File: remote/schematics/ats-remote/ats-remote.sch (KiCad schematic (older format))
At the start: 9 parts, among them J1 Conn_01x08, J2 Conn_01x08, J3 Conn_01x07, J4 Conn_01x07, J5 Conn_01x09, J6 Conn_01x09, U1 RFM95W-915S2, U2 PIC18F06Q40, U3 YIC71009EBGG

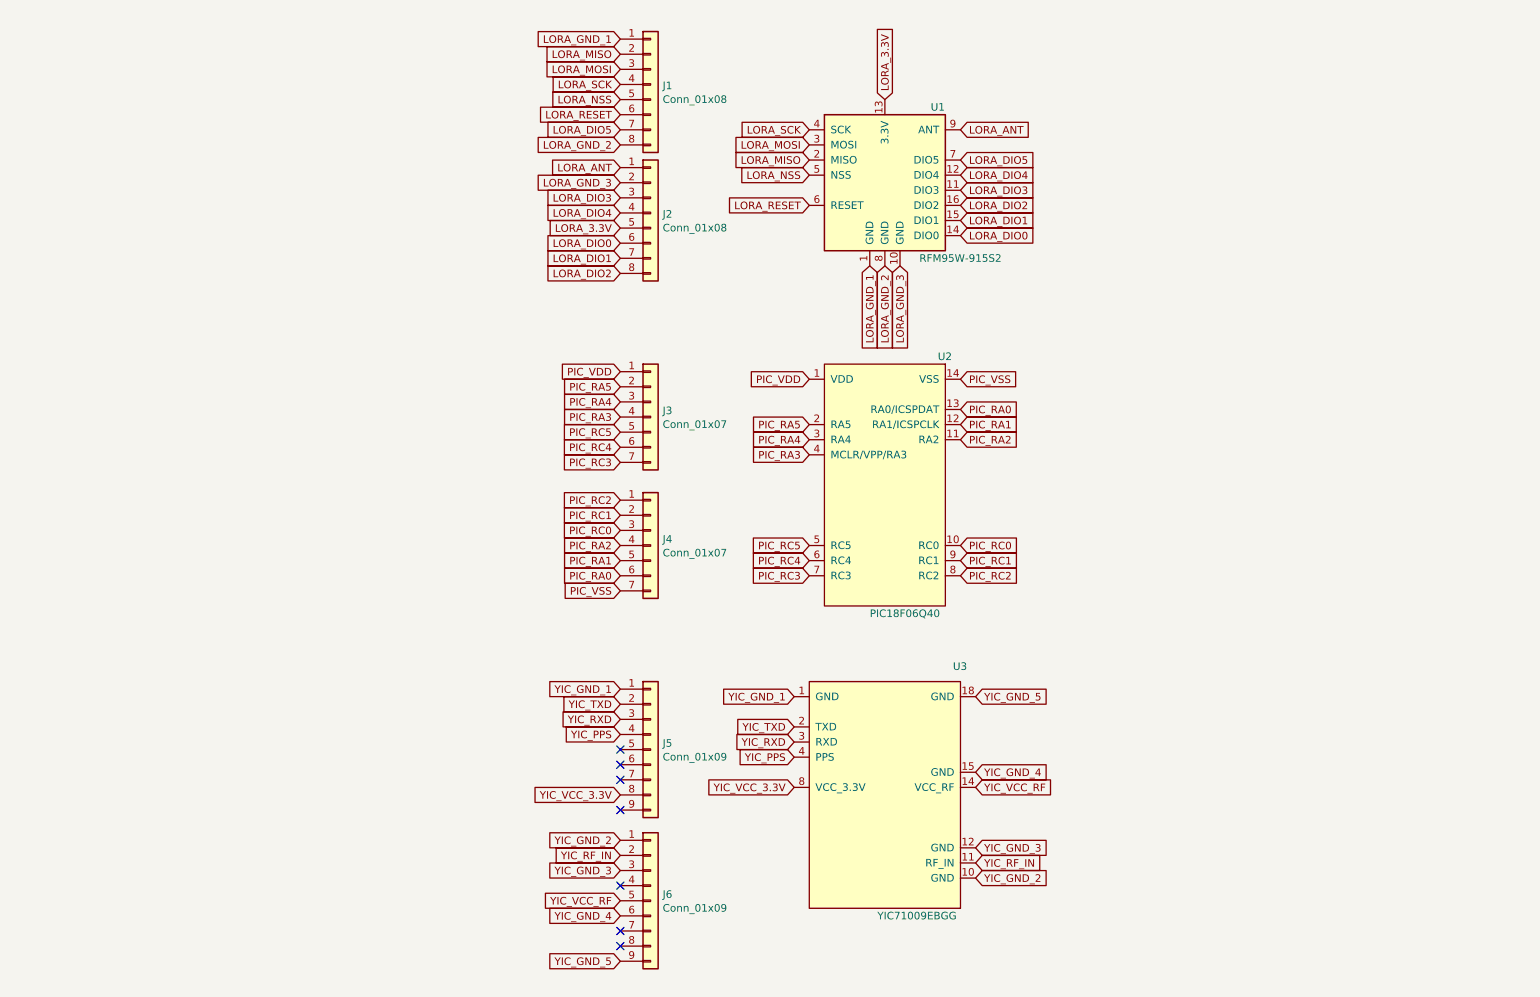
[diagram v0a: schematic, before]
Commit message: move remote schematic and pcb to v0.2.0 (#2)
v0.2.0

- 3.3v power and ground header
    - No OVP
    - No OCP
    - No polarity protection
    - Modules have their own decoupling caps
    - Modules have decoupling capacitors
- SPI header for LoRa module debug
- UART header for GPS module debug
- ICSP header for programming the PIC18
- LoRa module and SMD antenna
- GPS module and SMD antenna
- PIC18 controller
    - Controls SPI and UART
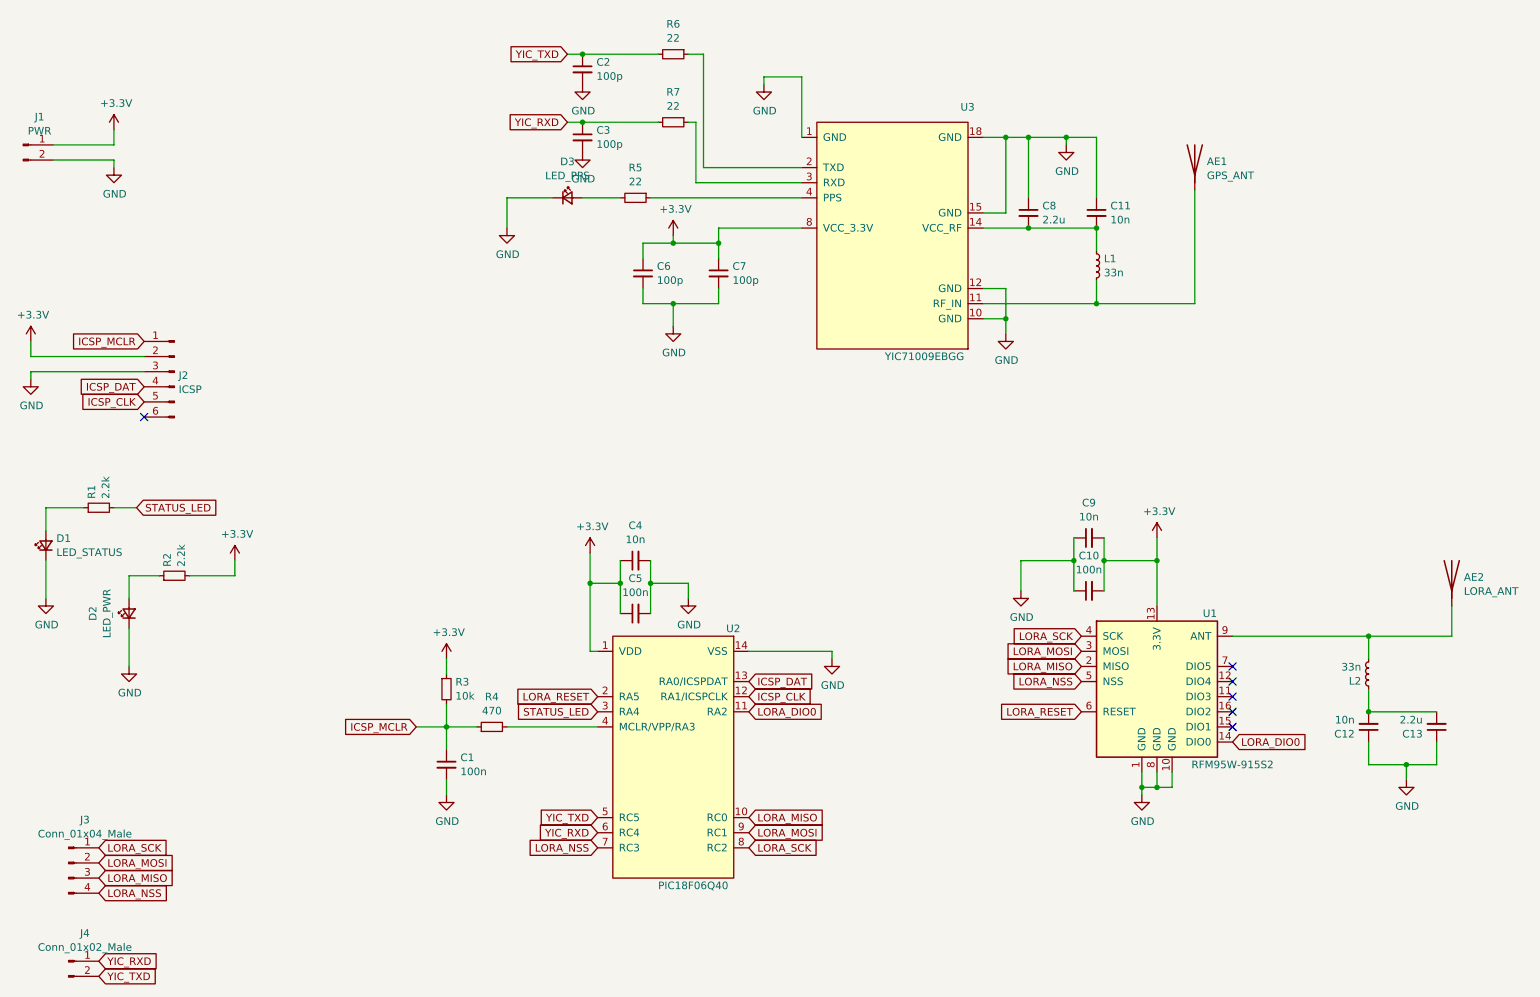
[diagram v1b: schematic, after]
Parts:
- removed J1, J2: Conn_01x08, Connector_PinSocket_1.27mm:PinSocket_1x08_P1.27mm_Vertical, symbol Connector_Generic:Conn_01x08
- removed J3, J4: Conn_01x07, Connector_PinSocket_1.27mm:PinSocket_1x07_P1.27mm_Vertical, symbol Connector_Generic:Conn_01x07
- removed J5, J6: Conn_01x09, Connector_PinSocket_1.27mm:PinSocket_1x09_P1.27mm_Vertical, symbol Connector_Generic:Conn_01x09
- added AE1: GPS_ANT, ats-remote:GPS_ANT_SR4G008, symbol Device:Antenna
- added AE2: LORA_ANT, ats-remote:LORA_ANT_YIC71009EBGG, symbol Device:Antenna
- added C1, C10, C5: 100n, Capacitor_SMD:C_0805_2012Metric_Pad1.18x1.45mm_HandSolder, symbol Device:C_Small
- added C11, C12, C4, C9: 10n, Capacitor_SMD:C_0805_2012Metric_Pad1.18x1.45mm_HandSolder, symbol Device:C_Small
- added C13, C8: 2.2u, Capacitor_SMD:C_0805_2012Metric_Pad1.18x1.45mm_HandSolder, symbol Device:C_Small
- added C2, C3, C6, C7: 100p, Capacitor_SMD:C_0805_2012Metric_Pad1.18x1.45mm_HandSolder, symbol Device:C_Small
- added D1: LED_STATUS, Diode_SMD:D_1206_3216Metric_Pad1.42x1.75mm_HandSolder, symbol Device:LED_Small
- added D2: LED_PWR, Diode_SMD:D_1206_3216Metric_Pad1.42x1.75mm_HandSolder, symbol Device:LED_Small
- added D3: LED_PPS, Diode_SMD:D_1206_3216Metric_Pad1.42x1.75mm_HandSolder, symbol Device:LED_Small
- added J1: PWR, Connector_PinHeader_1.27mm:PinHeader_1x02_P1.27mm_Vertical, symbol Connector:Conn_01x02_Male
- added J2: ICSP, Connector_PinHeader_1.27mm:PinHeader_1x06_P1.27mm_Vertical, symbol Connector:Conn_01x06_Male
- added J3: Conn_01x04_Male, Connector_PinHeader_1.27mm:PinHeader_1x04_P1.27mm_Vertical, symbol Connector:Conn_01x04_Male
- added J4: Conn_01x02_Male, Connector_PinHeader_1.27mm:PinHeader_1x02_P1.27mm_Vertical, symbol Connector:Conn_01x02_Male
- added L1, L2: 33n, Inductor_SMD:L_0603_1608Metric_Pad1.05x0.95mm_HandSolder, symbol Device:L_Small
- added R1, R2: 2.2k, Resistor_SMD:R_1206_3216Metric_Pad1.30x1.75mm_HandSolder, symbol Device:R_Small
- added R3: 10k, Resistor_SMD:R_1206_3216Metric_Pad1.30x1.75mm_HandSolder, symbol Device:R_Small
- added R4: 470, Resistor_SMD:R_1206_3216Metric_Pad1.30x1.75mm_HandSolder, symbol Device:R_Small
- added R5, R6, R7: 22, Resistor_SMD:R_1206_3216Metric_Pad1.30x1.75mm_HandSolder, symbol Device:R_Small
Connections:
- net LORA_GND_2 is gone; now on net GND: U1.8 (GND)
- net LORA_GND_3 is gone; now on net GND: U1.10 (GND)
- net PIC_RA2 is gone; now on net LORA_DIO0: U2.11 (RA2)
- net PIC_RA5 is gone; now on net LORA_RESET: U2.2 (RA5)
- net PIC_RC0 is gone; now on net LORA_MISO: U2.10 (RC0)
- net PIC_RC1 is gone; now on net LORA_MOSI: U2.9 (RC1)
- net PIC_RC2 is gone; now on net LORA_SCK: U2.8 (RC2)
- net PIC_RC3 is gone; now on net LORA_NSS: U2.7 (RC3)
- net PIC_RC4 is gone; now on net YIC_RXD: U2.6 (RC4)
- net PIC_RC5 is gone; now on net YIC_TXD: U2.5 (RC5)
- net PIC_VDD is gone; now on net +3V3: U2.1 (VDD)
- net PIC_VSS is gone; now on net GND: U2.14 (VSS)
- net YIC_GND_1 is gone; now on net GND: U3.1 (GND)
- net YIC_GND_2 is gone; now on net GND: U3.10 (GND)
- net YIC_GND_3 is gone; now on net GND: U3.12 (GND)
- net YIC_GND_4 is gone; now on net GND: U3.15 (GND)
- net YIC_GND_5 is gone; now on net GND: U3.18 (GND)
- net YIC_VCC_3.3V is gone; now on net +3V3: U3.8 (VCC_3.3V)
- net LORA_MISO: now also J3.3 (Pin_3)
- net LORA_MOSI: now also J3.2 (Pin_2)
- net LORA_NSS: now also J3.4 (Pin_4)
- net LORA_SCK: now also J3.1 (Pin_1)
- net YIC_RXD: now also C3.1, J4.1 (Pin_1), R7.2; no longer U3.3 (RXD)
- net YIC_TXD: now also C2.1, J4.2 (Pin_2), R6.2; no longer U3.2 (TXD)
- net LORA_3.3V renamed +3V3
- net +3V3: now also C10.2, C4.1, C5.1, C6.1, C7.1, C9.2, J1.1 (Pin_1), J2.2 (Pin_2), R2.2, R3.1
- net LORA_ANT: no longer names the net of U1.9 (ANT)
- net LORA_ANT: now also AE2.1 (A), L2.2
- net LORA_DIO1: no longer names the net of U1.15 (DIO1)
- net LORA_DIO2: no longer names the net of U1.16 (DIO2)
- net LORA_DIO3: no longer names the net of U1.11 (DIO3)
- net LORA_DIO4: no longer names the net of U1.12 (DIO4)
- net LORA_DIO5: no longer names the net of U1.7 (DIO5)
- net LORA_GND_1 renamed GND
- net GND: now also C1.2, C10.1, C11.1, C12.1, C13.1, C2.2, C3.2, C4.2, C5.2, C6.2, C7.2, C8.1, C9.1, D1.1 (K), D2.1 (K), D3.1 (K), J1.2 (Pin_2), J2.3 (Pin_3)
- net PIC_RA0 renamed ICSP_DAT
- net ICSP_DAT: now also J2.4 (Pin_4)
- net PIC_RA1 renamed ICSP_CLK
- net ICSP_CLK: now also J2.5 (Pin_5)
- net PIC_RA3: no longer names the net of U2.4 (MCLR/VPP/RA3)
- net PIC_RA3: now also R4.2
- net PIC_RA4 renamed STATUS_LED
- net STATUS_LED: now also R1.2
- net YIC_PPS: no longer names the net of U3.4 (PPS)
- net YIC_PPS: now also R5.1
- net YIC_RF_IN: no longer names the net of U3.11 (RF_IN)
- net YIC_RF_IN: now also AE1.1 (A), L1.2
- net YIC_VCC_RF: no longer names the net of U3.14 (VCC_RF)
- net YIC_VCC_RF: now also C11.2, C8.2, L1.1
- new net: R6.1, U3.2 (TXD)
- new net: R7.1, U3.3 (RXD)
- new net: D1.2 (A), R1.1
- new net: D2.2 (A), R2.1
- new net: D3.2 (A), R5.2
- new net: C12.2, C13.2, L2.1
- new net ICSP_MCLR: C1.1, J2.1 (Pin_1), R3.2, R4.1
- no-connect marks 7 -> 6
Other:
- moved on the sheet: U1, U2, U3
